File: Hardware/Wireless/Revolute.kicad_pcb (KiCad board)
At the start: 4 copper layers, 19.5 x 20 mm, 58 parts, among them U1 BQ27441-G1, U10 Button, U2 nrf52833_qfn40, U3 AS5600, U4 MIC5504, U5 BQ24075RGT, U6 Button, U7 Conn_01x14_Socket, U8 Button, U9 Button, X1 32.768 kHz, X2 32MHZ

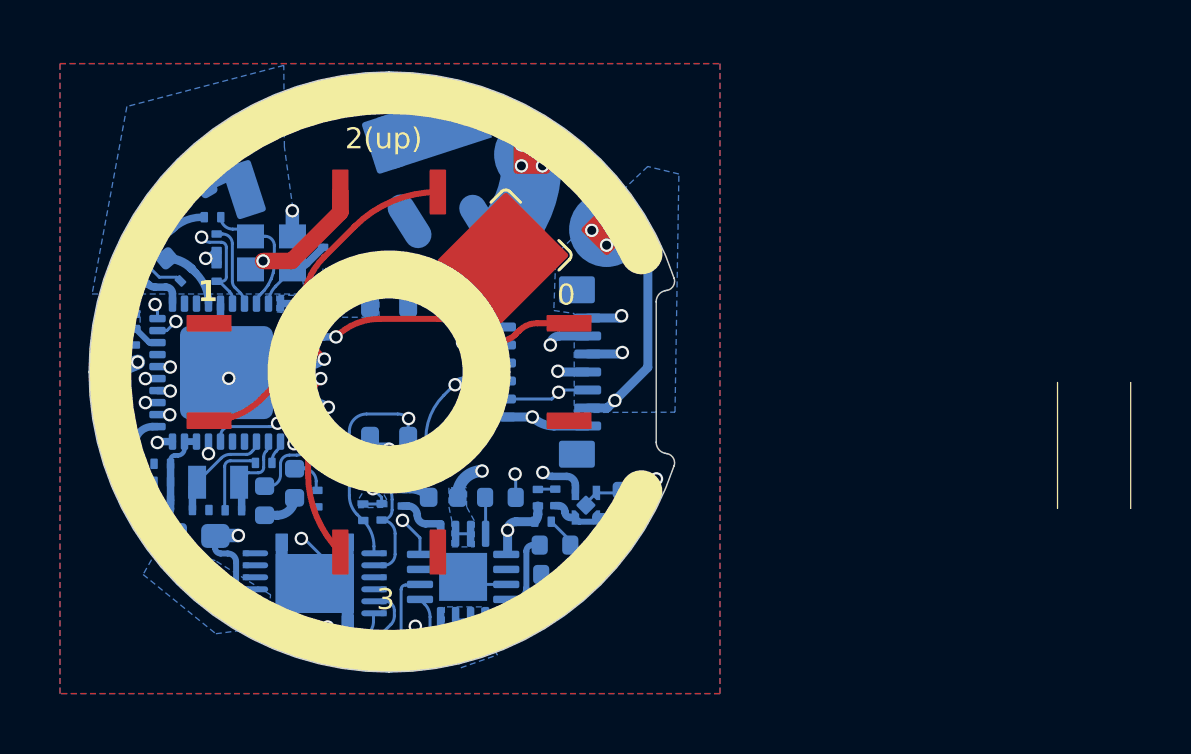
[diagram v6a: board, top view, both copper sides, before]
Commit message: added gyro, flex pcb antenna
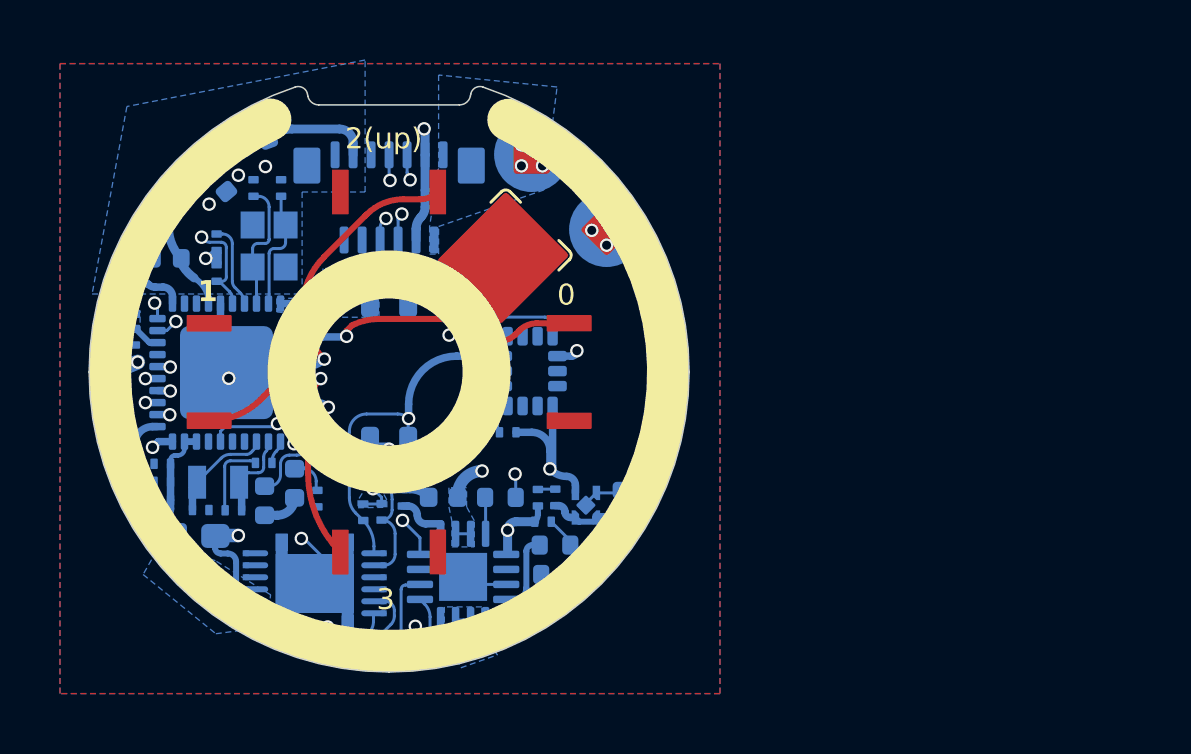
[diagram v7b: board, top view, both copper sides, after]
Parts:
- removed AE1: 2.4G ANT, Library:Antenna 2450AT42A100
- added R11: 10k, Library:Resistor-0201, B.Cu at (175.0, 97.0)
- added U11: LSM6DS3, Package_LGA:LGA-14_3x2.5mm_P0.5mm_LayoutBorder3x4y, B.Cu at (175.7, 95.0)
- C15, C19: footprint Library:Capacitor-0201 -> Library:Capacitor_0402_1005M-nosilk
- moved U7 7.80 mm to (171.0, 89.2), turned to 0 degrees
- moved REF** 3.54 mm to (175.8, 87.8)
- moved REF** 3.54 mm to (178.2, 90.2)
- moved L4 2.61 mm to (166.5, 87.4), turned to 20 degrees
- moved C16 2.20 mm to (167.4, 88.9)
- moved C19 2.20 mm to (165.3, 88.6)
- moved C17 1.68 mm to (166.5, 88.9), turned to -90 degrees
- moved L3 1.40 mm to (163.9, 89.6), turned to 55 degrees
- moved C15 0.86 mm to (163.6, 91.2), turned to 0 degrees
- moved X2 0.24 mm to (167.0, 90.8), turned to 90 degrees
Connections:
- L4 pad 2: Net-(AE1-A) -> antenna
- U2 pad 6: DIR -> int1
- U2 pad 7: ASOUT -> unconnected-(U2-P0.11-Pad7)
- U3 pad 3: ASOUT -> unconnected-(U3-OUT-Pad3)
- U3 pad 8: DIR -> unconnected-(U3-DIR-Pad8)
- U7 pad 1: swc -> GND
- U7 pad 10: GND -> Batteryin
- U7 pad 11: VBUS -> Batteryin
- U7 pad 12: Batteryin -> VBUS
- U7 pad 13: Batteryin -> VBUS
- U7 pad 2: swd -> GND
- U7 pad 3: D- -> antenna
- U7 pad 4: D+ -> GND
- U7 pad 5: RESET -> GND
- U7 pad 6: VDD_nRF -> D+
- U7 pad 7: P0.17 -> swc
- U7 pad 8: P0.15 -> D-
- U7 pad 9: GND -> swd
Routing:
- net ASOUT: track 18.8 -> 0.00 mm, vias 2 -> 0
- net RESET: track 17.6 -> 0.43 mm, vias 2 -> 1
- net GND: track 38.7 -> 23.5 mm
- net int1: track 0.00 -> 13.2 mm, vias 0 -> 2
- net Batteryin: track 9.82 -> 21.2 mm
- net swc: track 17.3 -> 11.4 mm
- net DIR: track 4.38 -> 0.00 mm, vias 2 -> 0
- net VDD_nRF: track 13.7 -> 17.5 mm
- net antenna: track 0.00 -> 3.58 mm
- net Net-(AE1-A): track 1.80 -> 0.00 mm
- net Net-(U11-CS): track 0.00 -> 1.64 mm
- net VBUS: track 29.4 -> 28.0 mm, vias 7 -> 6
- net Net-(U2-XC2): track 2.72 -> 4.03 mm
- net P0.15: track 22.3 -> 21.2 mm
- net D-: track 15.2 -> 14.3 mm
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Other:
- board size 19.5 x 20 mm -> 20 x 19.5 mm

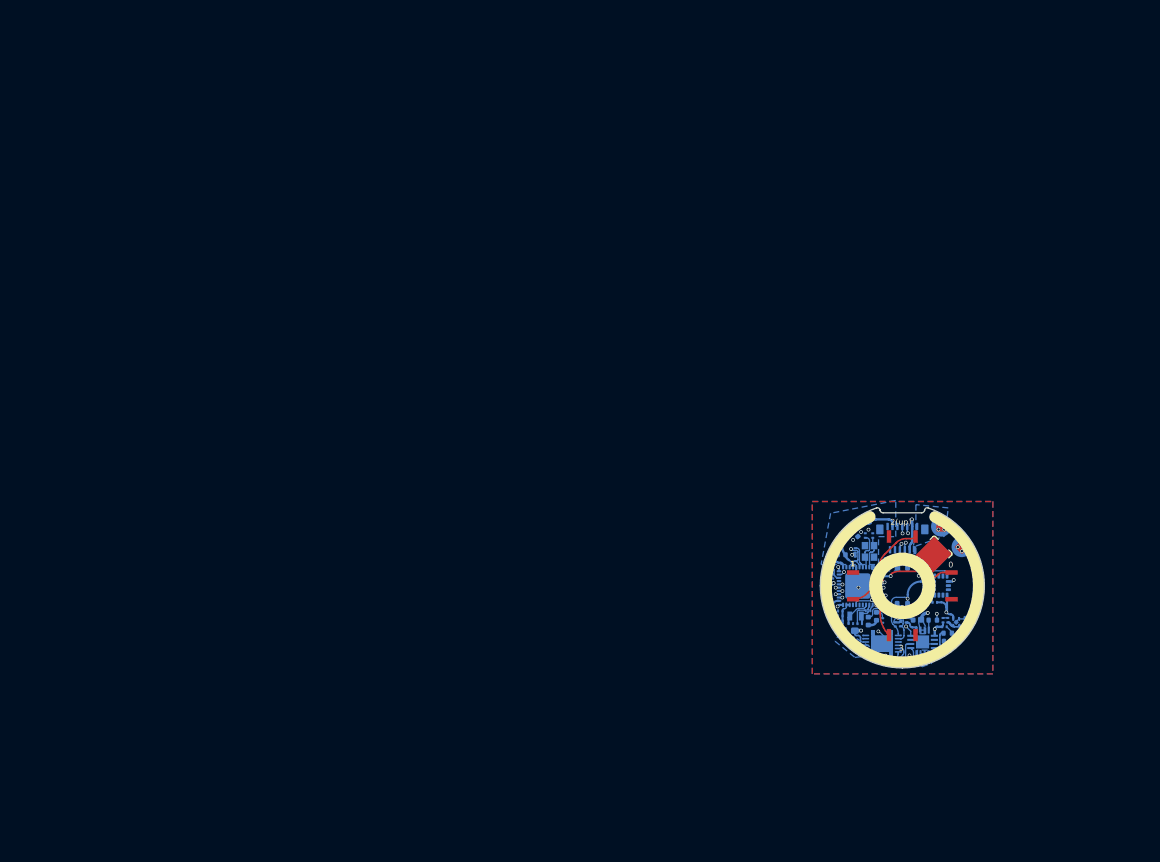
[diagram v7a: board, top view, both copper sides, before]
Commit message: revision 3, added mosfets for sensor power cutoff
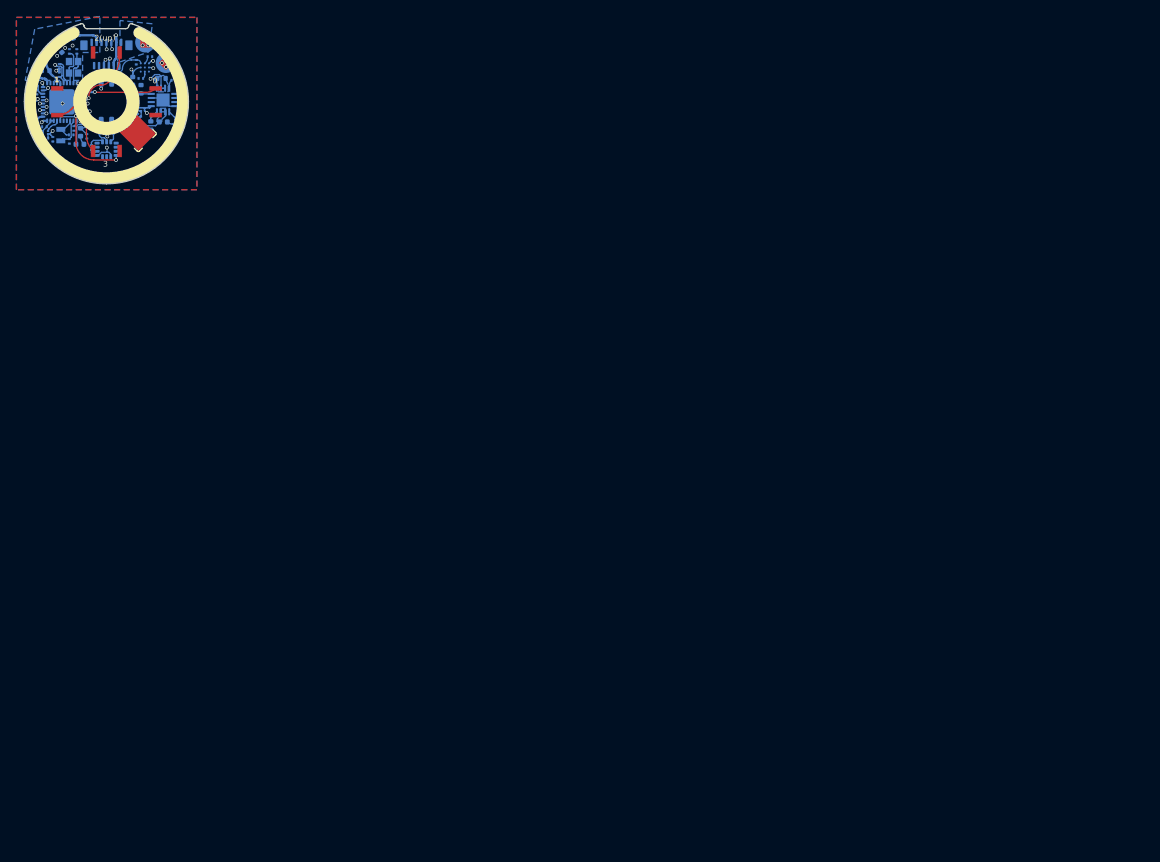
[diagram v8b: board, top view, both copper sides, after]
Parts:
- added Q1: NMOS, Library:Mosfet0402, B.Cu at (66.6, 39.7)
- C12: value 470nF -> 2.2uF
- R1: value 0.01 -> 10k; footprint Resistor_SMD:R_0603_1608Metric -> Library:Resistor-0201
- U1: value BQ27441-G1 -> ~; footprint Package_SON:Texas_S-PDSO-N12 -> Package_BGA:Texas_DSBGA-9_1.62mmx1.58mm_Layout3x3_P0.5mm
- U11: value LSM6DS3 -> LSM6DSO
- moved R5 118.6 mm to (78.2, 34.5), turned to 90 degrees
- moved C26 117.9 mm to (77.7, 38.7), turned to 180 degrees
- moved TH1 117.9 mm to (80.7, 33.2)
- moved C6 117.7 mm to (77.2, 36.2), turned to 90 degrees
- moved U4 117.5 mm to (77.7, 37.5), turned to 180 degrees
- moved C12 116.9 mm to (79.3, 30.5), turned to 0 degrees
- moved C4 116.8 mm to (77.6, 31.2), turned to -90 degrees
- moved R11 116.8 mm to (72.2, 41.6), turned to 90 degrees
- moved C24 116.8 mm to (77.8, 36.0)
- moved R3 115.3 mm to (82.2, 33.4), turned to 0 degrees
- moved C22 115.0 mm to (78.3, 39.5), turned to 0 degrees
- moved U11 114.7 mm to (74.0, 41.8), turned to 180 degrees
- moved R6 114.2 mm to (73.4, 39.9), turned to 180 degrees
- moved U1 114.0 mm to (78.7, 31.8), turned to 90 degrees
- moved U5 113.7 mm to (80.9, 35.8), turned to -90 degrees
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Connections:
- C20 pad 1: VDD_nRF -> MOS_VDD
- C21 pad 1: VDD_nRF -> MOS_VDD
- R1 pad 1: vBAT -> GND
- R1 pad 2: Batteryin -> Net-(U1-BIN)
- R11 pad 1: VDD_nRF -> MOS_VDD
- R6 pad 1: VDD_nRF -> MOS_VDD
- R8 pad 1: VDD_nRF -> MOS_VDD
- U11 pad 5: VDD_nRF -> MOS_VDD
- U11 pad 8: VDD_nRF -> MOS_VDD
- U2 pad 7: unconnected-(U2-P0.11-Pad7) -> MOS_EN
- U3 pad 1: VDD_nRF -> MOS_VDD
- U3 pad 2: VDD_nRF -> MOS_VDD
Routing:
- net MOS_VDD: track 0.00 -> 24.4 mm, vias 0 -> 4
- net Batteryin: track 21.2 -> 8.60 mm, vias 3 -> 1
- net GND: track 23.5 -> 12.0 mm, vias 17 -> 15
- net VDD_nRF: track 17.5 -> 7.04 mm, vias 7 -> 5
- net vBAT: track 1.50 -> 8.85 mm
- net OUT: track 10.5 -> 5.58 mm, vias 2 -> 0
- net VBUS: track 28.0 -> 31.4 mm
- net P0.15: track 21.2 -> 23.8 mm
- net Net-(U5-EN1): track 2.89 -> 1.01 mm
- net MOS_EN: track 0.00 -> 1.85 mm
- net Net-(U5-TS): track 2.90 -> 1.20 mm
- net Net-(U5-ISET): track 2.65 -> 1.26 mm
- net 1.8V: track 2.26 -> 0.91 mm
- net P0.17: track 25.5 -> 24.2 mm, vias 2 -> 3
- net Net-(U2-DCC): track 3.74 -> 4.80 mm
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- removed copper zone on In2.Cu, net Batteryin
- removed copper zone on In2.Cu, net vBAT
